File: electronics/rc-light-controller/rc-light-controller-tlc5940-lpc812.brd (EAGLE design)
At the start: 26.7 x 17.8 mm, 35 parts, among them U2 TLC5940PWP

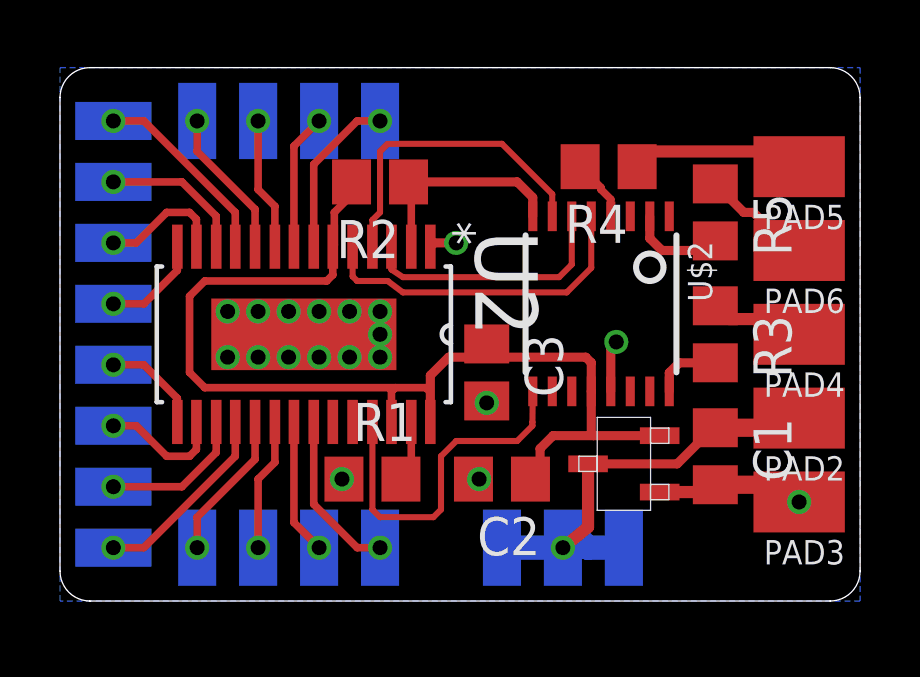
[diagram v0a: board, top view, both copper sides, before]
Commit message: Update LPC812 board
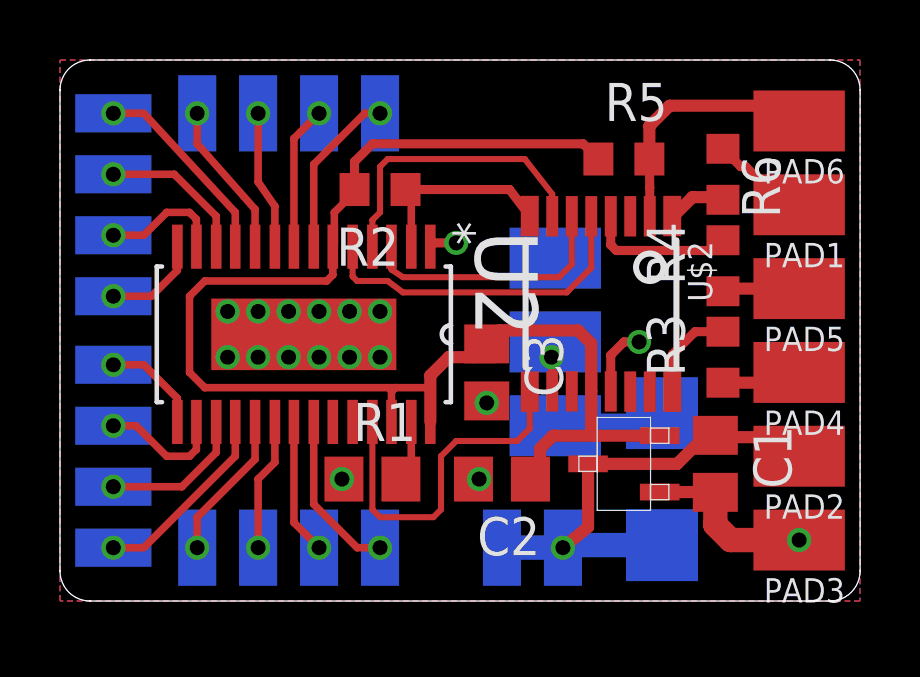
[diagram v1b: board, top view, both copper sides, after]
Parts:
- removed PAD24: (no value), wirepad:SMD50X100
- added D1: (Diode), diode:SMB
- added PAD1: CH3, wirepad:SMD80X120
- added PAD27: +5V, wirepad:SMD80X120
- added PAD28: Data out, wirepad:SMD80X120
- added PAD7: GND, wirepad:SMD80X120
- added R6: 1k, rcl:R0603
- PAD6: value CH3/ISP -> OUT/ISP
- R2: value 10k-100k -> 33k; device rcl:R0805 -> rcl:R0603
- R3, R4: device rcl:R0805 -> rcl:R0603
- R5: value 1k -> 33k; device rcl:R0805 -> rcl:R0603
- U$2: device LPC800:TSSOP16 -> LPC810:TSSOP16
- moved R4 5.04 mm to (22.1, 11.2), turned to 90 degrees
- moved PAD6 4.32 mm to (24.6, 16.0)
- moved PAD5 4.06 mm to (24.6, 10.4)
- moved R5 3.53 mm to (18.8, 14.7), turned to 0 degrees
- moved PAD2 1.27 mm to (24.6, 4.83)
- moved PAD4 1.27 mm to (24.6, 7.62)
- moved PAD3 1.27 mm to (24.6, 2.03)
- moved R3 0.80 mm to (22.1, 8.13), turned to 90 degrees
- moved PAD10 0.25 mm to (6.60, 16.3)
- moved PAD11 0.25 mm to (4.57, 16.3)
- moved PAD12 0.25 mm to (1.78, 16.3)
- moved PAD8 0.25 mm to (10.7, 16.3)
- moved PAD9 0.25 mm to (8.64, 16.3)
- moved R2 0.25 mm to (10.7, 13.7)
- moved C1 0.25 mm to (21.8, 4.57)
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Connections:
- removed net N$19: PAD6.1, R5.1
- new net N$1: PAD1.1, R6.1
- new net N$2: R6.2, U$2.1
- new net N$3: D1.C, PAD27.1
- new net N$5: PAD28.1, U$2.10
- net +3V3: now also R5.1
- net GND: now also PAD7.1
- net N$20: now also PAD6.1
- net VIN: now also D1.A; no longer PAD24.1
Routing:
- net +3V3: track 37.3 -> 47.9 mm
- net N$20: track 3.22 -> 8.70 mm
- net N$19: track 3.81 -> 0.00 mm
- net N$1: track 0.00 -> 3.80 mm
- net N$3: track 0.00 -> 3.73 mm
- net N$18: track 6.03 -> 3.06 mm
- net ST/CLK/RX: track 2.08 -> 5.04 mm
- net N$2: track 0.00 -> 1.99 mm
- net VIN: track 15.2 -> 16.9 mm
- net N$5: track 0.00 -> 1.67 mm, vias 0 -> 1
- net GND: track 9.18 -> 10.2 mm, vias 19 -> 18
- net TH/DAT/TX: track 2.29 -> 3.24 mm
- net SCLK: track 10.6 -> 9.93 mm
- net BLANK: track 7.15 -> 6.54 mm
- added copper zone on layer 1, net GND
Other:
- board size 26.7 x 17.8 mm -> 26.7 x 18 mm
- board text added: "+LED"
- board text added: "0"
- board text added: "1"
- board text added: "10"
- board text added: "12"
- board text added: "13"
- board text added: "14"
- board text added: "15"
- board text added: "2"
- board text added: "3"
- board text added: "5"
- board text added: "6"
- board text added: "7"
- board text added: "8"
- board text added: "9"
- board text added: "WS2812"
